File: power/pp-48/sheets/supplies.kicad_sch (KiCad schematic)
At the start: 17 parts, among them U1 LM5164DDA

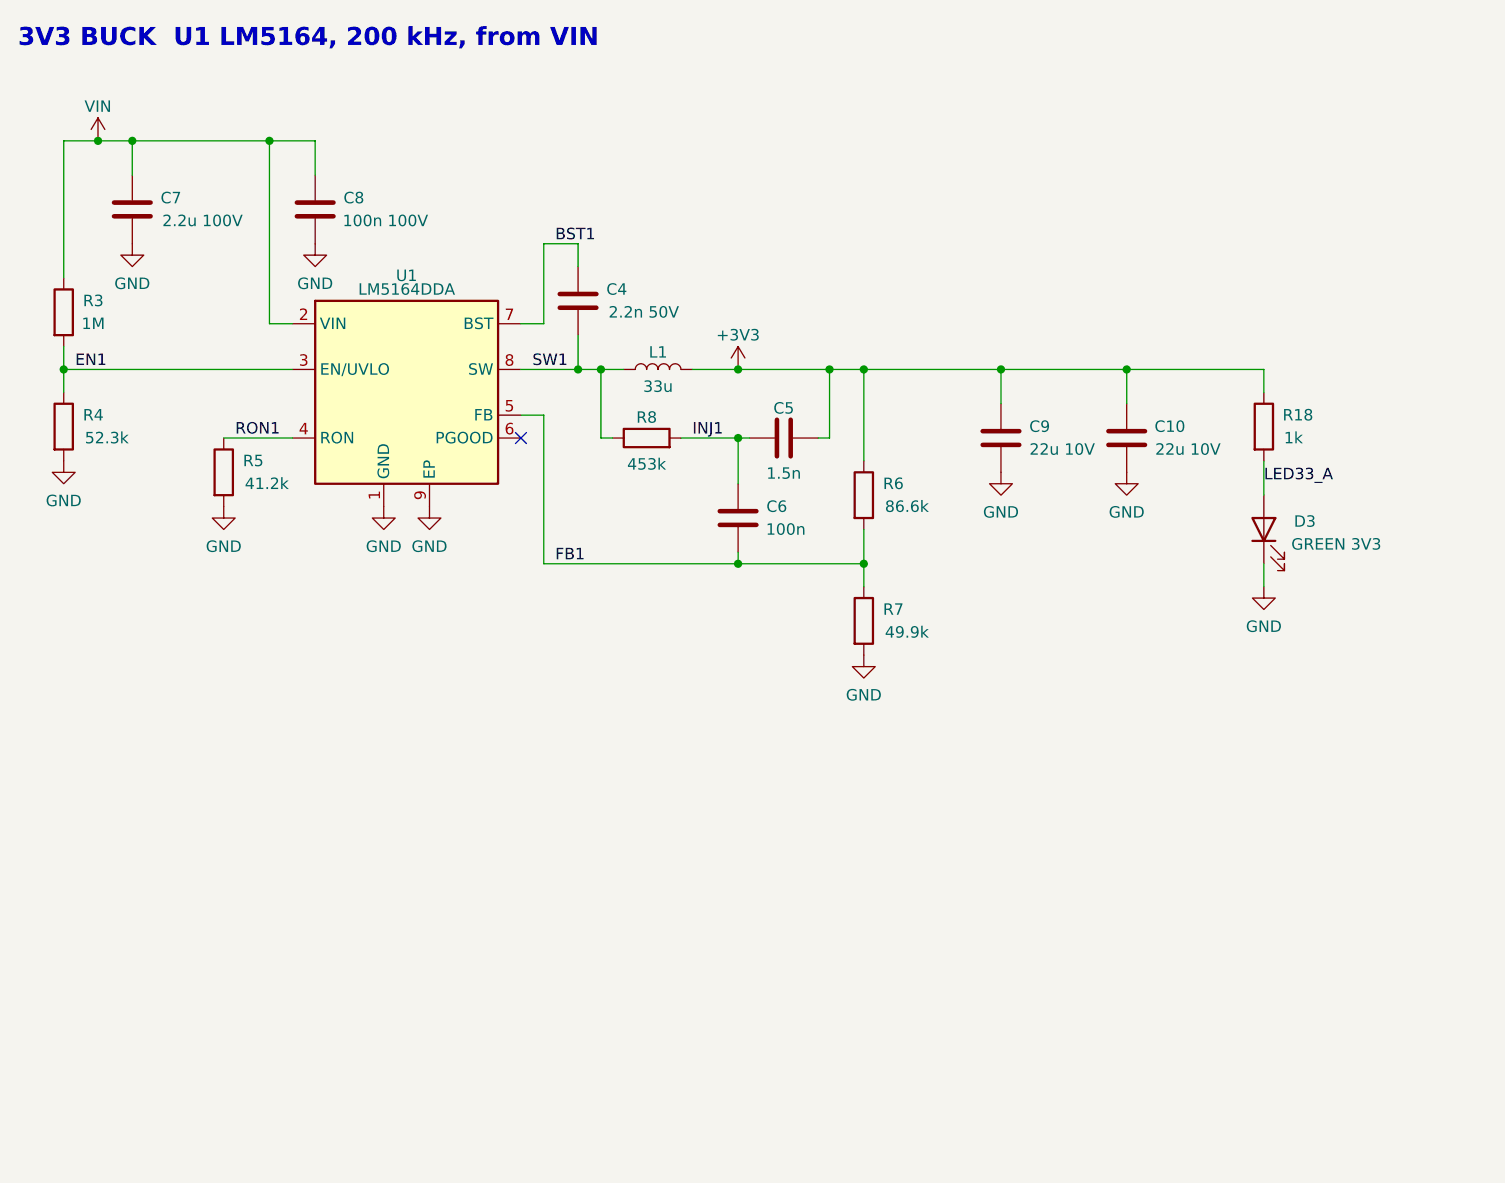
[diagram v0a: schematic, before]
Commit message: pp-48: Supplies sheet gets the isolated 12 V aux as an INTERIM off-the-shelf module (U2 URB4812YMD-6WR3 class, 6 W, 1.5 kV, LCSC C5369743; Cin 22u + 2.2u 100V, Cout 10u, LED, J4 JST PH CTRL_12V / CTRL_GND), standing in for the own Fly-Buck until an isolated coupled inductor is found at LCSC; pp:DCDC_Iso_1x1_Single symbol and pp48:Converter_DCDC_1x1in_THT footprint; ERC only the input-sheet labels; ADR 0003 decision 14 and handoff note the revisit
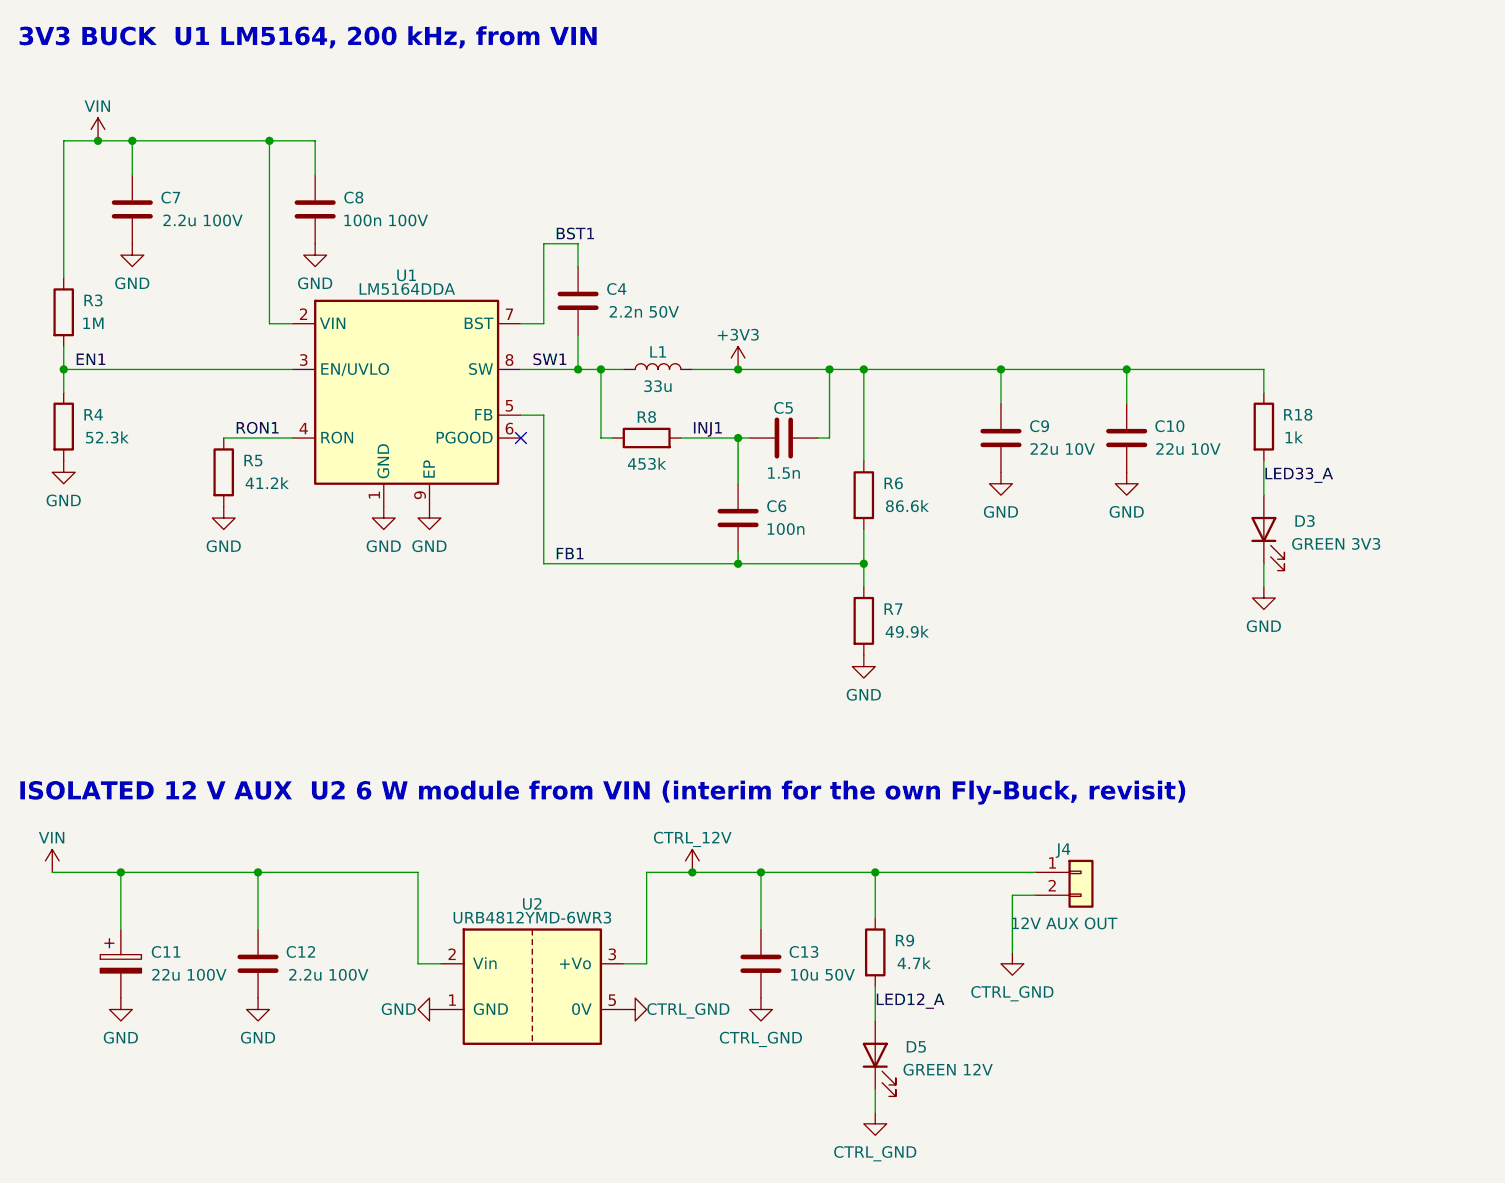
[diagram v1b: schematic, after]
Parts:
- added C11: 22u 100V, Capacitor_SMD:CP_Elec_10x10, symbol Device:C_Polarized
- added C12: 2.2u 100V, Capacitor_SMD:C_1210_3225Metric, symbol Device:C
- added C13: 10u 50V, Capacitor_SMD:C_1210_3225Metric, symbol Device:C
- added D5: GREEN 12V, LED_SMD:LED_0603_1608Metric, symbol Device:LED
- added J4: 12V AUX OUT, Connector_JST:JST_PH_B2B-PH-K_1x02_P2.00mm_Vertical, symbol Connector_Generic:Conn_01x02
- added R9: 4.7k, Resistor_SMD:R_0603_1608Metric, symbol Device:R
- added U2: URB4812YMD-6WR3, pp48:Converter_DCDC_1x1in_THT, symbol pp:DCDC_Iso_1x1_Single
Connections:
- net GND: now also C11.2, C12.2, U2.1 (GND)
- net VIN: now also C11.1, C12.1, U2.2 (Vin)
- new net CTRL_12V: C13.1, J4.1 (Pin_1), R9.1, U2.3 (+Vo)
- new net CTRL_GND: C13.2, D5.1 (K), J4.2 (Pin_2), U2.5 (0V)
- new net LED12_A: D5.2 (A), R9.2
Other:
- note added: "ISOLATED 12 V AUX U2 6 W module from VIN (interim for the own Fly-Buck, revisit)"
